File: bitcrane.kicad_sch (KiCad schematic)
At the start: 125 parts, among them J1 0455580003, J10 PSU Comm, J11 0353180420, J12 0353180420, J13 0353180420, J14 0353180420, J15 Conn_01x04, J2 USB_C_Receptacle_USB2.0, J3 2x9P 2mm, J4 2x9P 2mm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

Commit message: drc check. copy over missing footprints to bitcrane library
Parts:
- removed TP10, TP11, TP12, TP13, TP14, TP15, TP16, TP17, TP18, TP27, TP28, TP5, TP6, TP7, TP8, TP9: TestPoint, TestPoint:TestPoint_Pad_D1.5mm, symbol Connector:TestPoint
- C1, C4: footprint Capacitor_SMD:C_0805_2012Metric -> Capacitor_SMD:C_0402_1005Metric; LCSC C28233 -> (none)
- C2, C3: footprint Capacitor_SMD:C_0805_2012Metric -> Capacitor_SMD:C_0402_1005Metric; LCSC C28323 -> (none)
- J2: footprint aditBoard:USB_C_Receptacle_GCT_USB4105-xx-A_16P_TopMnt_Horizontal -> bitcrane:USB_C_Receptacle_GCT_USB4105-xx-A_16P_TopMnt_Horizontal
- R17, R19, R22, R23, R26, R27, R29, R30, R31: footprint Resistor_SMD:R_0805_2012Metric -> Resistor_SMD:R_0402_1005Metric; LCSC C60816 -> (none)
- R18, R20, R21, R24, R25, R28, R32, R33, R34: footprint Resistor_SMD:R_0805_2012Metric -> Resistor_SMD:R_0402_1005Metric; LCSC C17673 -> (none)
- R3: footprint Resistor_SMD:R_0805_2012Metric -> Resistor_SMD:R_0402_1005Metric; LCSC C17444 -> (none)
- U3: footprint emberone:USON-8_UX_2x3x0p6_WIN -> bitcrane:USON-8_UX_2x3x0p6_WIN
- U6: footprint Package_DFN_QFN:QFN-56-1EP_7x7mm_P0.4mm_EP3.2x3.2mm -> bitcrane:QFN-56-1EP_7x7mm_P0.4mm_EP3.2x3.2mm
- U7: footprint emberone:LED-SMD_4P-L4.0-W1.6-L -> bitcrane:LED-SMD_4P-L4.0-W1.6-L
- Y1: footprint emberone:XTAL_ECS-120-20-33-CKM-TR3 -> bitcrane:XTAL_ECS-120-20-33-CKM-TR3

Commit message: change buttons to LCSC versions. add preliminary LCSC part numbers for everything
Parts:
- C1, C4: LCSC (none) -> C307331; PARTNO CL21B104KCFNNNE -> KGM05AR71C104KH
- C2, C3: LCSC (none) -> C52923; PARTNO CL21B105KAFNNNE -> EMK105BJ105MV-F
- D1: LCSC (none) -> C364284
- D3, D4, D5, D6: LCSC (none) -> C165455
- Q2, Q3, Q4, Q5: LCSC (none) -> C5248642
- R1: PARTNO RC0402FR-0710KL -> RC0402JR-0710KL
- R10, R11, R12, R9: LCSC (none) -> C106235
- R13, R14, R15, R16: LCSC (none) -> C25744
- R17, R18, R19, R20, R21, R22, R23, R24, R25, R26, R27, R28, R29, R30, R31, R32, R33, R34: LCSC (none) -> C25900; PARTNO RC0805FR-074K7L -> (none)
- R3: LCSC (none) -> C25752; PARTNO RMCF0805FT12K0 -> (none)
- R6: LCSC (none) -> C25897
- SW1, SW2: value GT-TC029B-H025-L1N -> TS-1088-AR02016; footprint bitaxe:SW_CS1213AGF260_CRS -> bitcrane:SW-SMD_L3.9-W3.0-P4.45; DK 2449-CS1213AGF260CT-ND -> (none); LCSC (none) -> C720477; LCSC Part (none) -> C720477; PARTNO CS1213AGF260 -> (none)
- U1, U2: LCSC (none) -> C3702980
- U4: LCSC (none) -> C15578

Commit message: removed old libraries
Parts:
- C1, C4: DK 1276-6840-1-ND -> (none); PARTNO KGM05AR71C104KH -> (none)
- C10, C8: DK 490-5935-1-ND -> (none); Manufacturer FH(风华) -> (none); PARTNO GRM1555C1H300JA01D -> (none)
- C11, C12, C15, C16, C17, C18, C19, C20, C21, C7: DK 478-KGM05AR71C104KHCT-ND -> (none); Manufacturer SAMSUNG(三星) -> (none); PARTNO KGM05AR71C104KH -> (none)
- C13, C14: DK 587-5514-1-ND -> (none); Manufacturer SAMSUNG(三星) -> (none); PARTNO EMK105BJ105MV-F -> (none)
- C2, C3: DK 1276-1066-1-ND -> (none); PARTNO EMK105BJ105MV-F -> (none)
- C5: DK 490-18663-1-ND -> (none); PARTNO GRM21BR61H106KE43L -> (none)
- D1: DK SMBJP6KE6.8A-TPMSCT-ND -> (none); PARTNO SMBJP6KE6.8A-TP -> (none)
- D2: symbol Diode:BZX84Cxx -> bitcrane:BZX84Cxx; PARTNO LBZX84C12LT1G -> (none)
- D3, D4, D5, D6: DK DDZ9684-7DICT-ND -> (none); PARTNO DDZ9684-7 -> (none)
- J1: symbol bitcart:0455580003 -> bitcrane:0455580003; DK WM10869-ND -> (none); PARTNO 0455580003 -> (none)
- J10: footprint bitcart:CONN-TH_6P-P2.00_PHD-2X3A -> bitcrane:CONN-TH_6P-P2.00_PHD-2X3A; DK S9470-ND -> (none); PARTNO SWR204-NRTN-D03-ST-GA -> (none)
- J11, J12: DK WM13195-ND -> (none); PARTNO 0353180420 -> (none)
- J2: symbol aditBoard:USB_C_Receptacle_USB2.0 -> bitcrane:USB_C_Receptacle_USB2.0; DK 2073-USB4105-GF-ACT-ND -> (none); PARTNO USB4105-GF-A -> (none)
- J3, J4, J5: footprint bitcart:CONN-TH_X2026WV-2-09D-46SN -> bitcrane:CONN-TH_X2026WV-2-09D-46SN; PARTNO X2026WV-2x09D-46SN -> (none)
- J8, J9: DK 732-2701-ND -> (none); PARTNO 61900411021 -> (none)
- Q1: DK DMP3013SFV-7DICT-ND -> (none); PARTNO DMP3013SFV-7 -> (none)
- Q2, Q3, Q4, Q5: DK BSS138K-13DICT-ND -> (none); PARTNO BSS138K-13 -> (none)
- R1: DK 311-10.0KLRCT-ND -> (none); PARTNO RC0402JR-0710KL -> (none)
- R10, R11, R12, R5, R9: DK 311-1.00KLRCT-ND -> (none); PARTNO RC0402FR-071KL -> (none)
- R13, R14, R15, R16: DK 311-10KJRCT-ND -> (none); PARTNO RC0402JR-0710KL -> (none)
- R17, R18, R19, R20, R21, R22, R23, R24, R25, R26, R27, R28, R29, R30, R31, R32, R33, R34: DK 311-4.70KCRCT-ND -> (none)
- R2, R4: DK RMCF0402JT5K10CT-ND -> (none); PARTNO RMCF0402JT5K10 -> (none)
- R3: DK RMCF0805FT12K0CT-ND -> (none)
- R6: DK 311-49.9KLRCT-ND -> (none); PARTNO RC0402FR-0749K9L -> (none)
- R7, R8: DK 311-33.0LRCT-ND -> (none); Manufacturer UNI-ROYAL(厚声) -> (none); PARTNO RC0402FR-0733RL -> (none)
- SW1, SW2: footprint bitcrane:SW-SMD_L3.9-W3.0-P4.45 -> bitaxe:SW_CS1213AGF260_CRS; DK (none) -> 2449-CS1213AGF260CT-ND; LCSC Part C720477 -> (none); PARTNO (none) -> CS1213AGF260
- U1, U2: symbol Power_Protection:TPD1E05U06DYA -> bitcrane:TPD1E05U06DYA; DK 296-TPD1E05U06DYARCT-ND -> (none); PARTNO TPD1E05U06DYAR -> (none)
- U3: symbol emberone:W25Q16JVUXIQ_TR -> bitcrane:W25Q16JVUXIQ_TR; DK 256-W25Q16JVUXIQTRCT-ND -> (none); PARTNO W25Q16JVUXIQ TR -> (none)
- U6: footprint bitcrane:QFN-56-1EP_7x7mm_P0.4mm_EP3.2x3.2mm -> Package_DFN_QFN:QFN-56-1EP_7x7mm_P0.4mm_EP3.2x3.2mm
- U7: symbol athvfd:SK6812SIDE-A-RVS -> bitcrane:SK6812SIDE-A-RVS; DK 1528-4691-ND-$$$$$ -> (none); PARTNO SK6812SIDE-A-RVS -> (none)
- Y1: symbol Device:Crystal_GND24_common -> bitcrane:Crystal_GND24_common; DK 50-ECS-120-20-33-CKM-TR3CT-ND -> (none); PARTNO ECS-120-20-33-CKM-TR3 -> (none)
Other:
- moved on the sheet: J15, TP4

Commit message: update test points and cleanup silkscreen. add render to readme.
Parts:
- D3, D4, D5, D6: LCSC C165455 -> C2112
- R17, R19, R22, R23, R26, R27, R29, R30, R31: now left out of the parts list
- SW1, SW2: footprint bitaxe:SW_CS1213AGF260_CRS -> bitcrane:SW-SMD_L3.9-W3.0-P4.45; DK 2449-CS1213AGF260CT-ND -> (none); PARTNO CS1213AGF260 -> (none)
- TP1: value TestPoint -> 5V; footprint TestPoint:TestPoint_Pad_D1.5mm -> bitcrane:TestPoint_Pad_D1.0mm
- TP19: value TestPoint -> SDA; footprint TestPoint:TestPoint_Pad_D1.5mm -> bitcrane:TestPoint_Pad_D1.0mm
- TP2: value TestPoint -> 3V3; footprint TestPoint:TestPoint_Pad_D1.5mm -> bitcrane:TestPoint_Pad_D1.0mm
- TP20: value TestPoint -> SCL; footprint TestPoint:TestPoint_Pad_D1.5mm -> bitcrane:TestPoint_Pad_D1.0mm
- TP21, TP23, TP25, TP32: value TestPoint -> PWM; footprint TestPoint:TestPoint_Pad_D1.5mm -> bitcrane:TestPoint_Pad_D1.0mm
- TP22, TP24, TP26, TP33: value TestPoint -> TACH; footprint TestPoint:TestPoint_Pad_D1.5mm -> bitcrane:TestPoint_Pad_D1.0mm
- TP29, TP30: footprint TestPoint:TestPoint_Pad_D1.5mm -> bitcrane:TestPoint_Pad_D1.0mm
- TP3: value TestPoint -> 12V; footprint TestPoint:TestPoint_Pad_D1.5mm -> bitcrane:TestPoint_Pad_D1.0mm
- TP31: value TestPoint -> GND; footprint TestPoint:TestPoint_Pad_D1.5mm -> bitcrane:TestPoint_Pad_D1.0mm
- TP4: value TestPoint -> PSU_EN; footprint TestPoint:TestPoint_Pad_D1.5mm -> bitcrane:TestPoint_Pad_D1.0mm
- U4: DK 296-28778-1-ND -> (none); PARTNO TLV1117LV33DCYR -> (none)
- U6: footprint Package_DFN_QFN:QFN-56-1EP_7x7mm_P0.4mm_EP3.2x3.2mm -> bitcrane:QFN-56-1EP_7x7mm_P0.4mm_EP3.2x3.2mm; DK 2648-SC0914(13)CT-ND -> (none); PARTNO SC0914(13) -> (none)
- U7: LCSC C2890037 -> C5378737

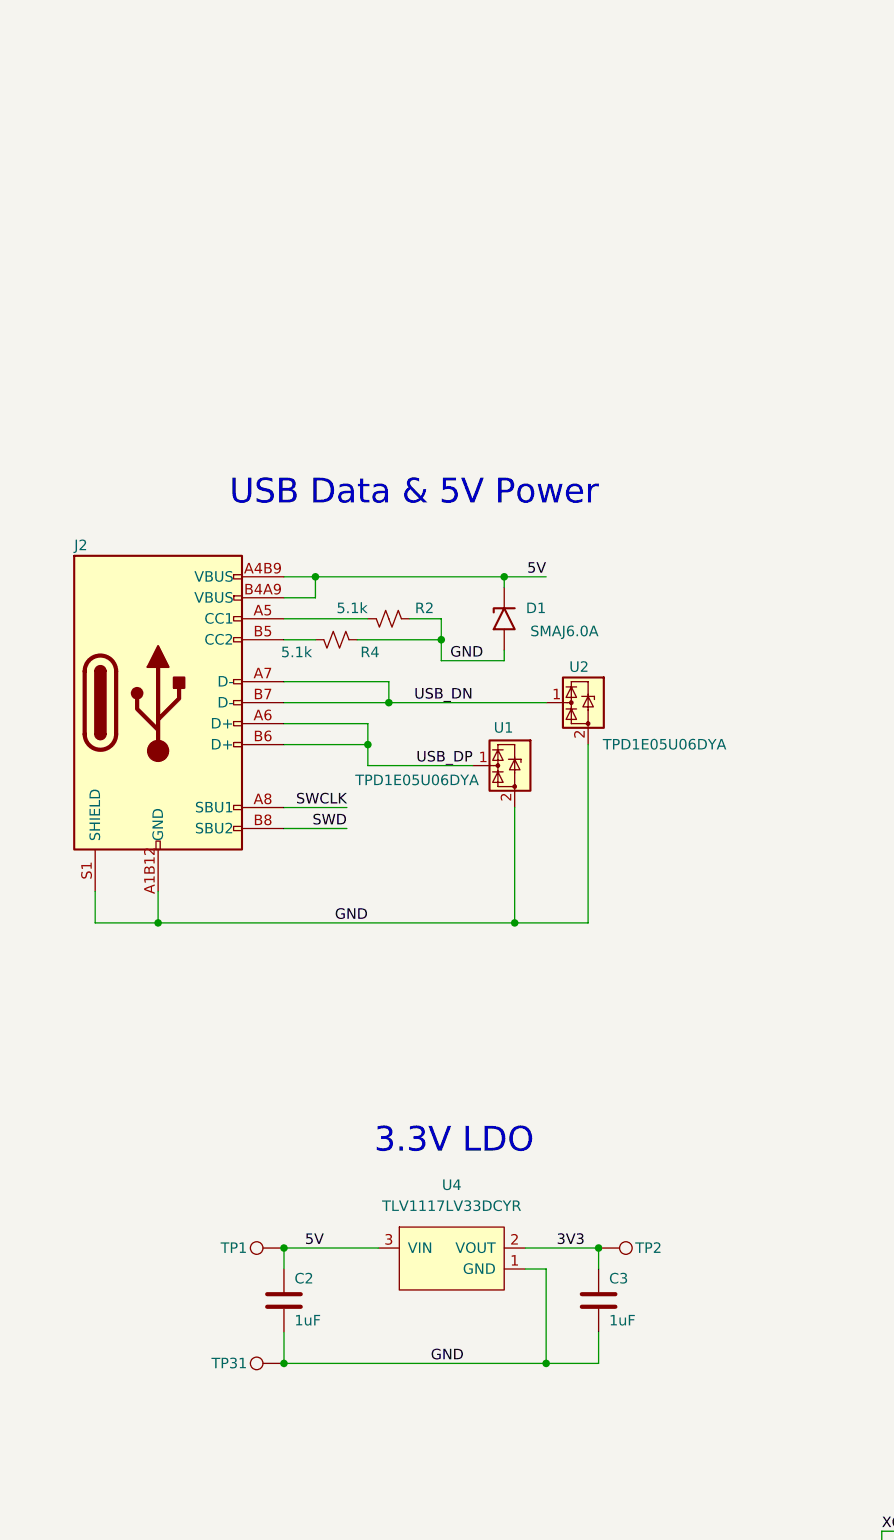
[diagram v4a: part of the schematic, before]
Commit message: add SWD header for #14
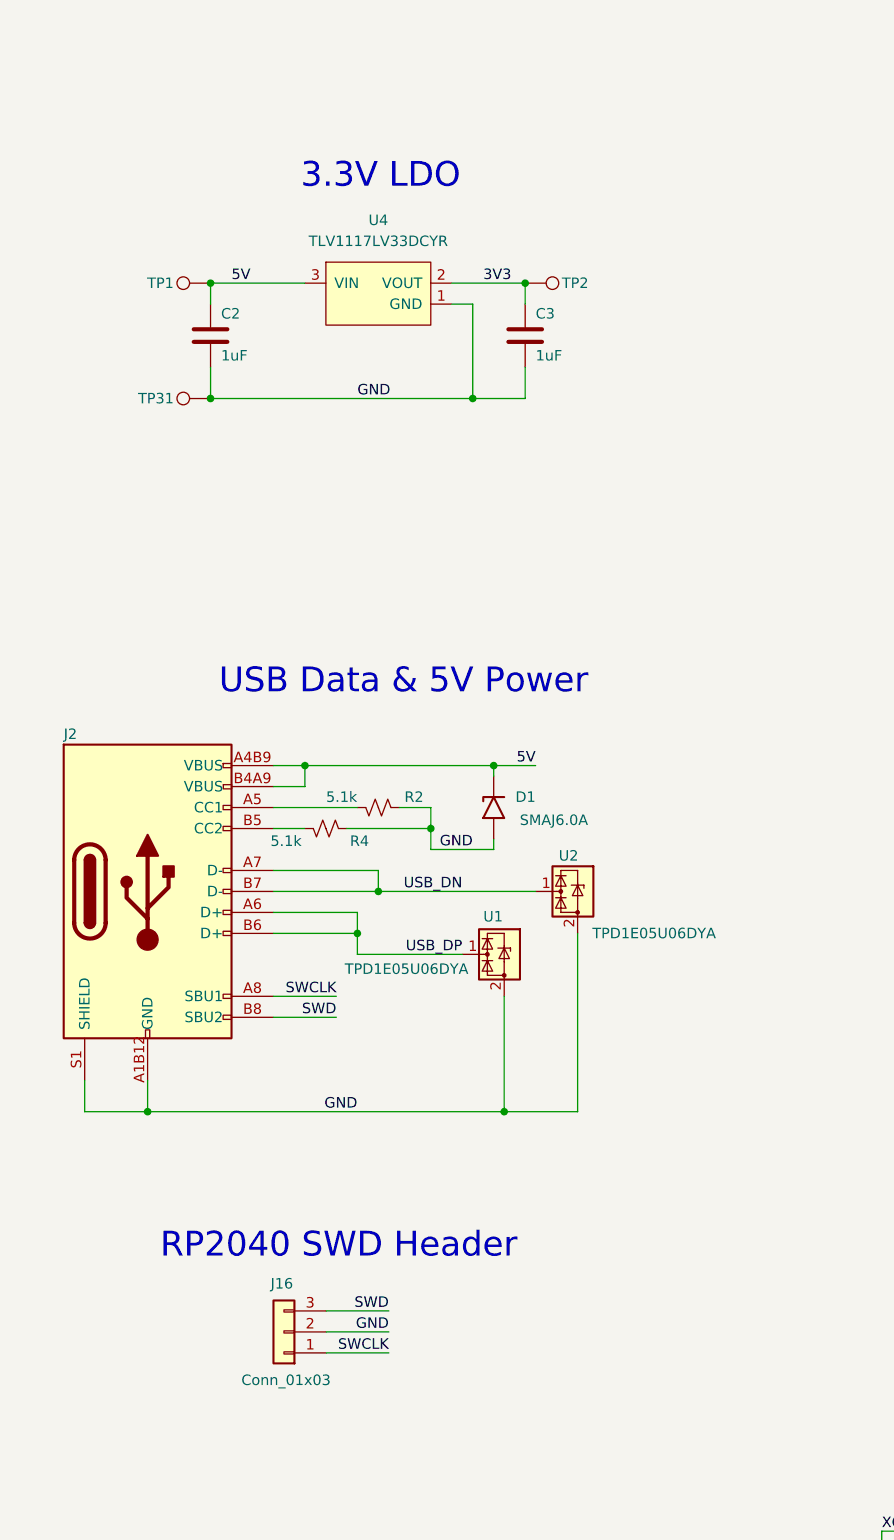
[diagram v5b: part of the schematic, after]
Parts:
- added J16: Conn_01x03, Connector_PinHeader_2.54mm:PinHeader_1x03_P2.54mm_Vertical, symbol Connector_Generic:Conn_01x03
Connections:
- net GND: now also J16.2 (Pin_2)
- net SWCLK: now also J16.1 (Pin_1)
- net SWD: now also J16.3 (Pin_3)
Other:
- note added: "RP2040 SWD Header"
- moved on the sheet: C2, C3, D1, J2, R2, R4, TP1, TP2, TP31, U1, U2, U4
